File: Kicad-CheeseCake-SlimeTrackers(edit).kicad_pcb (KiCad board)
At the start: 2 copper layers, 50 x 60 mm, 30 parts, among them J2 USB_C-16p, J3 4P4C, Q1 UMH3N, SW1 SW_SPDT, U1 ICM-45686, U2 TP4057, U3 CH340K, U4 ME6211C33M5

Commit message: updt
lots of fixes to footprints
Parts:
- ESP1: footprint SlimeFootprints:ESP12F-Devkit-V3 -> SlimeFootprints:ESP-12F
- L1: footprint LED_SMD:LED_RGB_Cree-PLCC-6_6x5mm_P2.1mm -> SlimeFootprints:LED_CLMVC-FKA-CG1H1A1BB7D3C3
- moved ESP1 68.1 mm to (80.4, 125.1), turned to 0 degrees
- moved U2 55.5 mm to (141.1, 105.2)
- moved U3 44.7 mm to (133.9, 105.0)
- moved L1 44.5 mm to (109.5, 110.6)
- moved R8 39.6 mm to (132.8, 116.6)
- moved R9 39.4 mm to (132.8, 119.1)
- moved U1 37.3 mm to (141.3, 131.9)
- moved C1 35.7 mm to (124.8, 114.1)
- moved R10 35.5 mm to (132.8, 121.6)
- moved C2 35.4 mm to (124.8, 116.6)
- moved B1 33.6 mm to (137.1, 115.1)
- moved J1 30.8 mm to (141.7, 115.1)
- moved R4 28.2 mm to (128.8, 124.1)
- moved J3 27.6 mm to (125.9, 156.8)
- moved U4 27.3 mm to (137.0, 137.4)
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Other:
- outline, holes or cut-outs redrawn

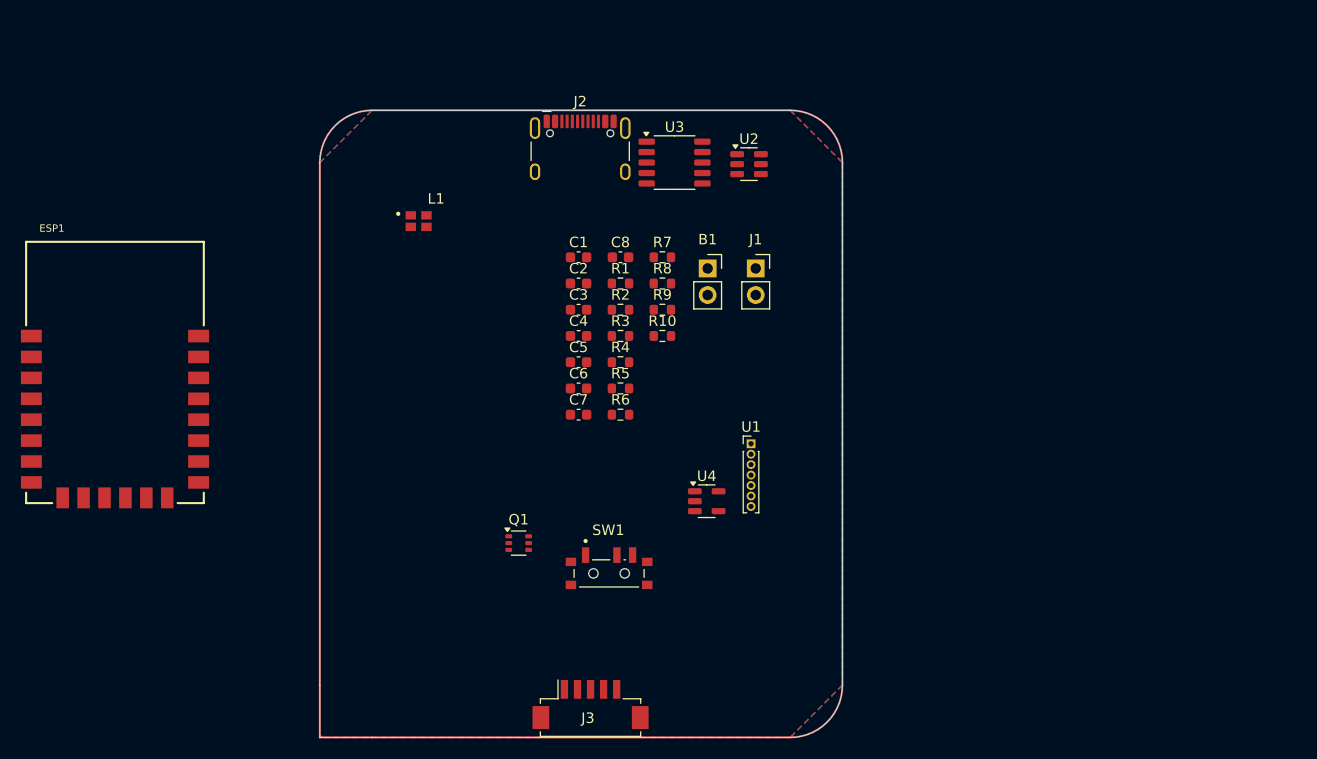
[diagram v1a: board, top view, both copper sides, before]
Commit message: fixes
board will be 33x35 or bigger
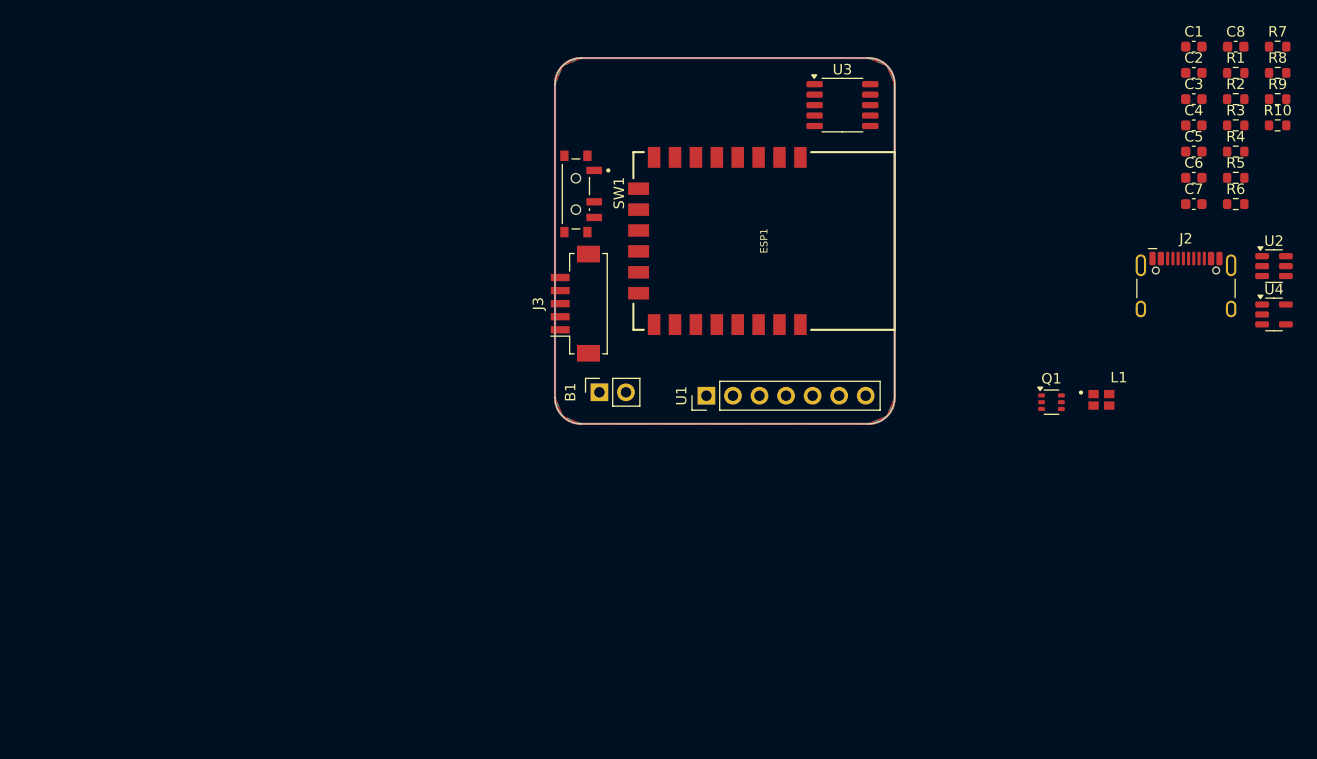
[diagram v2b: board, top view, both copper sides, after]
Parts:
- removed J1: ~, Connector_PinSocket_2.54mm:PinSocket_1x02_P2.54mm_Vertical
- U1: footprint Connector_PinHeader_1.00mm:PinHeader_1x07_P1.00mm_Vertical -> Connector_PinHeader_2.54mm:PinHeader_1x07_P2.54mm_Vertical
- moved L1 67.5 mm to (174.8, 127.7)
- moved ESP1 63.4 mm to (142.5, 112.5), turned to -90 degrees
- moved C1 62.2 mm to (183.6, 93.9)
- moved C2 62.2 mm to (183.6, 96.4)
- moved C3 62.2 mm to (183.6, 98.9)
- moved C4 62.2 mm to (183.6, 101.4)
- moved C5 62.2 mm to (183.6, 104.0)
- moved C6 62.2 mm to (183.6, 106.5)
- moved C7 62.2 mm to (183.6, 109.0)
- moved C8 62.2 mm to (187.6, 93.9)
- moved R1 62.2 mm to (187.6, 96.4)
- moved R2 62.2 mm to (187.6, 98.9)
- moved R3 62.2 mm to (187.6, 101.4)
- moved R4 62.2 mm to (187.6, 104.0)
- moved R5 62.2 mm to (187.6, 106.5)
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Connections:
- L1 pad 3: BAT+ -> +5V
- U2 pad 4: BAT+ -> +5V
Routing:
- added copper zone on B.Cu, net (none)
- added copper zone on F.Cu, net (none)
- removed copper zone on B.Cu, net GND
- removed copper zone on F.Cu, net GND
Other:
- board size 50 x 60 mm -> 32.5 x 35 mm

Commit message: updt
updt
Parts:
- ESP1: moved to B.Cu
- moved U2 63.3 mm to (130.4, 97.5)
- moved R8 63.2 mm to (132.3, 118.2), turned to 90 degrees
- moved R10 62.2 mm to (129.4, 101.6), turned to 90 degrees
- moved U4 61.7 mm to (131.0, 106.5)
- moved R7 61.2 mm to (137.0, 121.5), turned to 180 degrees
- moved R9 60.3 mm to (131.4, 101.6), turned to 90 degrees
- moved C1 59.2 mm to (124.8, 100.4), turned to 90 degrees
- moved L1 57.8 mm to (125.8, 97.0)
- moved C5 57.1 mm to (126.7, 100.4), turned to 90 degrees
- moved R6 55.9 mm to (133.2, 121.5), turned to 180 degrees
- moved R5 54.6 mm to (134.3, 118.2), turned to 90 degrees
- moved R4 53.4 mm to (135.1, 113.7)
- moved R3 53.3 mm to (135.1, 110.7)
- moved C8 53.1 mm to (134.9, 100.1)
- moved C6 53.0 mm to (131.1, 113.7)
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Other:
- outline, holes or cut-outs redrawn
